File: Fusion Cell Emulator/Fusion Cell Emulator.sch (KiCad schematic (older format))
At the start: 106 parts, among them J1 BINDING_POST_RED, J2 BINDING_POST_BLACK, J3 JST-XH, J4 0.1\" FEMALE HEADER, J6 BINDING_POST_RED, J7 BINDING_POST_BLACK, U1 LM317, U10 LM317, U11 LM317, U12 LM317, U13 LM317, U2 LM317, U3 LM317, U4 LM317, U5 LM317, U6 LM317, U7 LM317, U8 LM317, U9 LM317

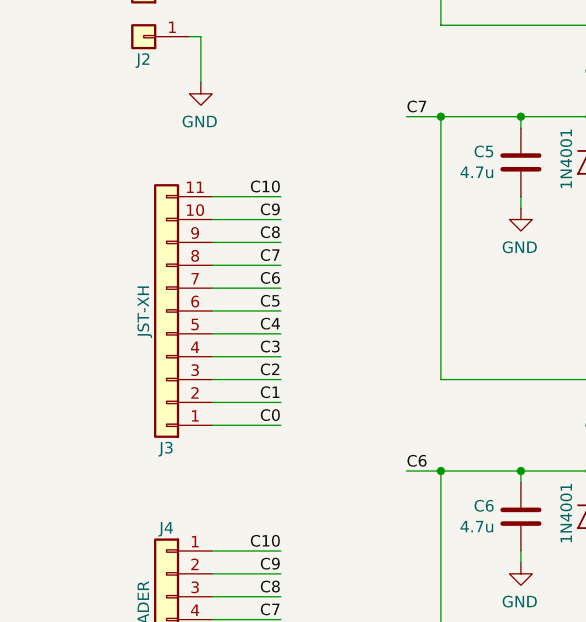
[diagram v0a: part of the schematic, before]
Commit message: Fixed JST orietation and Final Gerbers
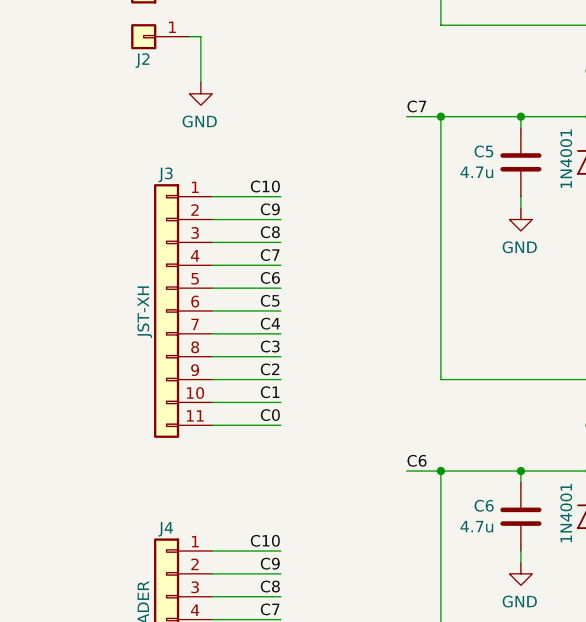
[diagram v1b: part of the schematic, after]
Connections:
- net C1: now also J3.10 (Pin_10); no longer J3.2 (Pin_2)
- net C10: now also J3.1 (Pin_1); no longer J3.11 (Pin_11)
- net C2: now also J3.9 (Pin_9); no longer J3.3 (Pin_3)
- net C3: now also J3.8 (Pin_8); no longer J3.4 (Pin_4)
- net C4: now also J3.7 (Pin_7); no longer J3.5 (Pin_5)
- net C6: now also J3.5 (Pin_5); no longer J3.7 (Pin_7)
- net C7: now also J3.4 (Pin_4); no longer J3.8 (Pin_8)
- net C8: now also J3.3 (Pin_3); no longer J3.9 (Pin_9)
- net C9: now also J3.2 (Pin_2); no longer J3.10 (Pin_10)
- net GND: now also J3.11 (Pin_11); no longer J3.1 (Pin_1)
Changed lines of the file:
@@
 F 3 "~" H 1300 6850 50  0001 C CNN
 	1    1300 6850
-	-1   0    0    1
+	-1   0    0    -1
 $EndComp
 $EndSCHEMATC

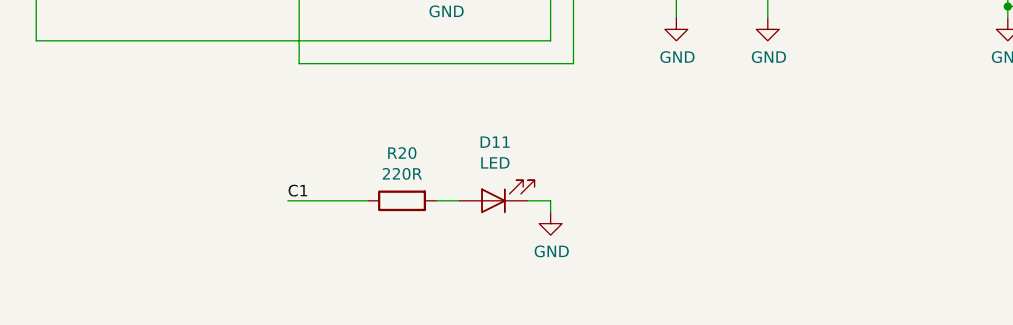
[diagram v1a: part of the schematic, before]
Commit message: Updated Pics, added shunt bodge resistor note
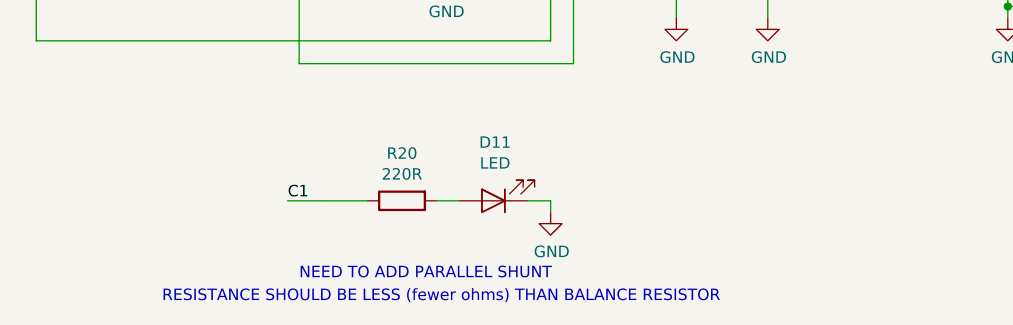
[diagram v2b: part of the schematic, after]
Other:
- note added: "NEED TO ADD PARALLEL SHUNT"
- note added: "RESISTANCE SHOULD BE LESS (fewer ohms) THAN BALANCE RESISTOR"
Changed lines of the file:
@@
 	-1   0    0    -1
 $EndComp
+Text Notes 3650 9750 0    50   ~ 0
+NEED TO ADD PARALLEL SHUNT
+Text Notes 3050 9850 0    50   ~ 0
+RESISTANCE SHOULD BE LESS (fewer ohms) THAN BALANCE RESISTOR
 $EndSCHEMATC
